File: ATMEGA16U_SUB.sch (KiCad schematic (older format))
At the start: 14 parts, among them J2 ICSP1, U5 ATmega16U2-MU, Y1 16MHz

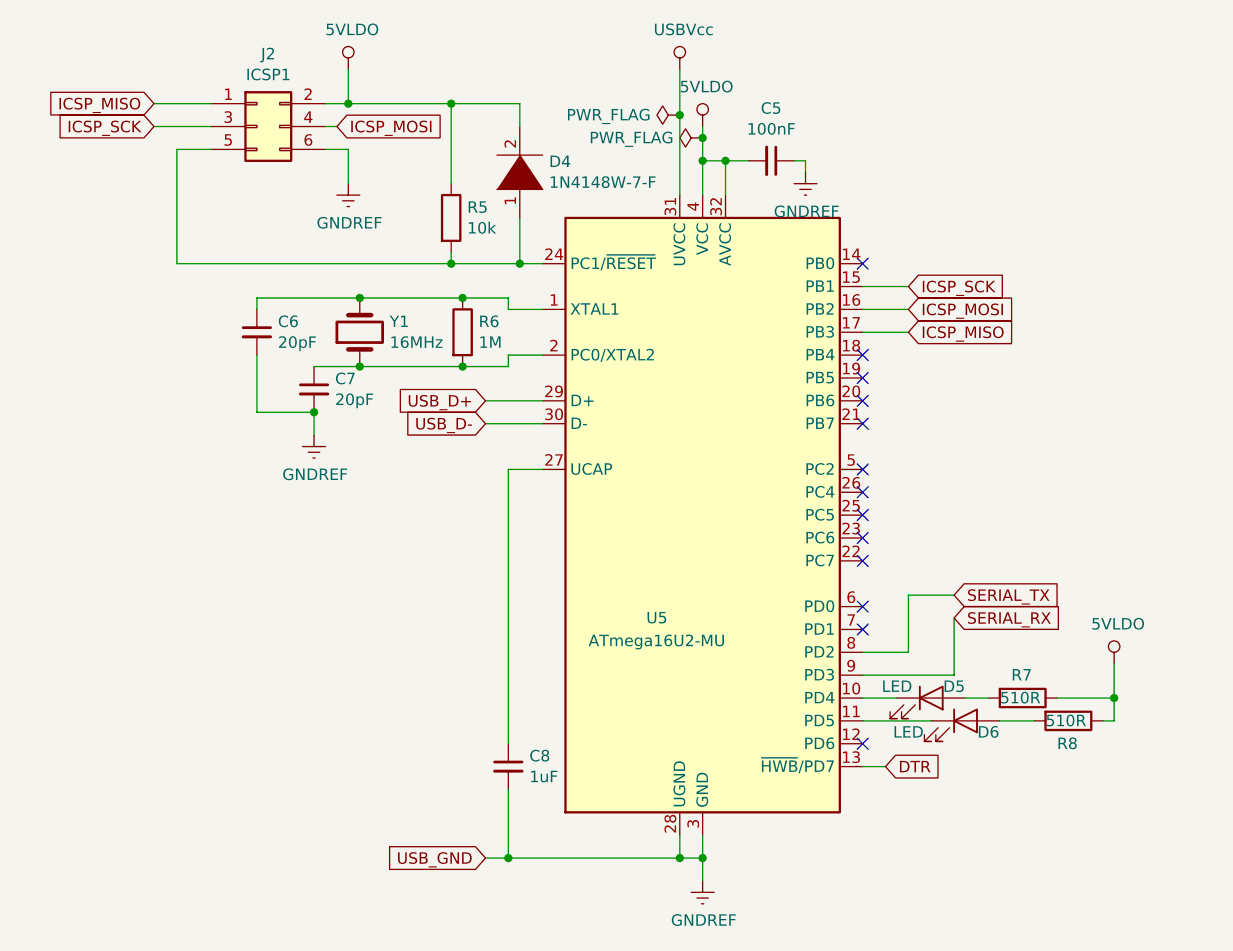
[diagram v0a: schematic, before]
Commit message: Set component footprints, added datasheets, fixed the last DRC error and a couple component values
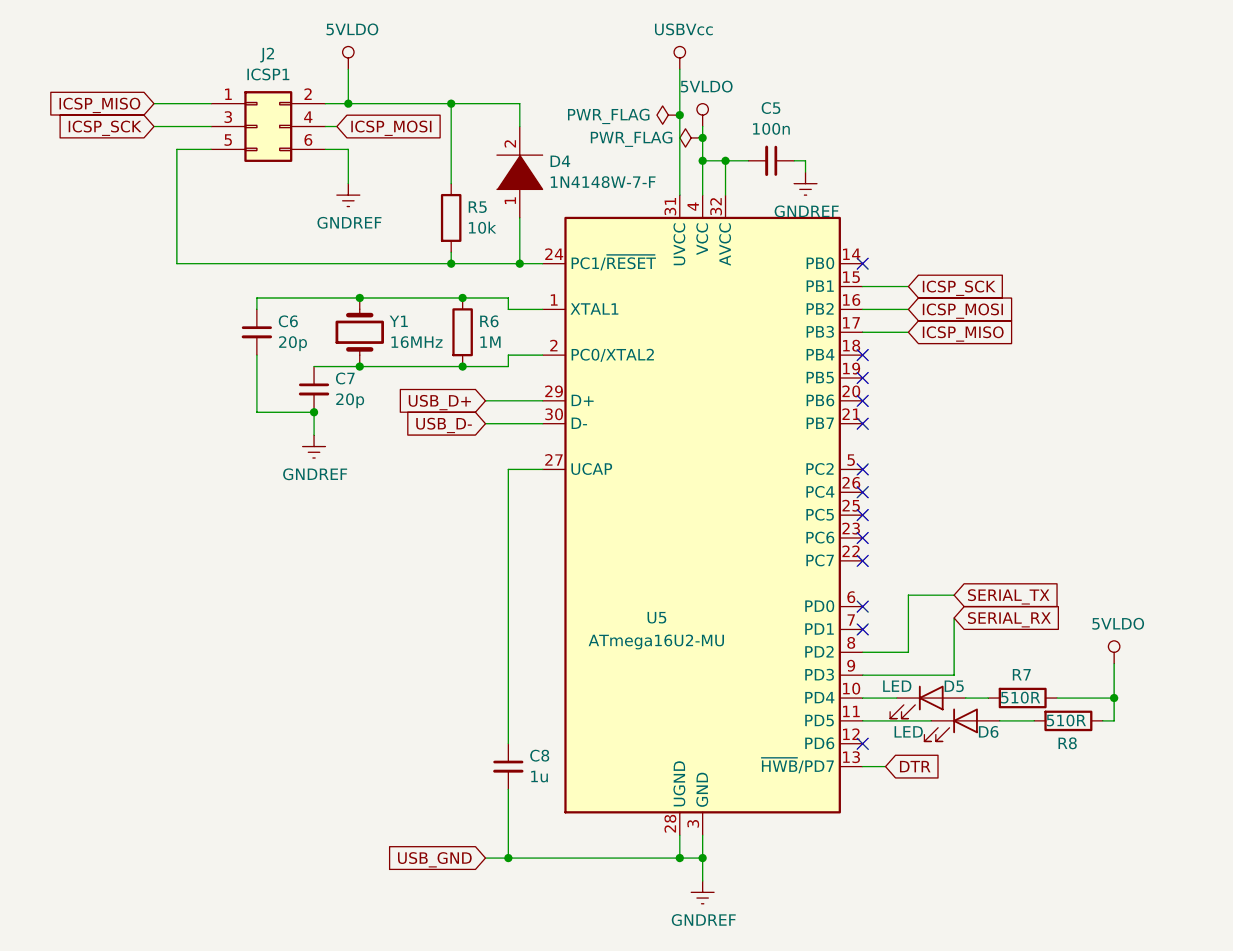
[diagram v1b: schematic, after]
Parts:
- C5: value 100nF -> 100n; footprint (none) -> Capacitor_SMD:C_0603_1608Metric
- C6, C7: value 20pF -> 20p; footprint (none) -> Capacitor_SMD:C_0603_1608Metric
- C8: value 1uF -> 1u; footprint (none) -> Capacitor_SMD:C_0603_1608Metric
- D4: footprint (none) -> Diode_SMD:D_SOD-123
- D5, D6: footprint (none) -> Diode_SMD:D_0603_1608Metric
- J2: footprint (none) -> Connector_PinHeader_2.54mm:PinHeader_2x03_P2.54mm_Vertical
- R5, R6, R7, R8: footprint (none) -> Resistor_SMD:R_0603_1608Metric
- Y1: footprint (none) -> Crystal:Crystal_SMD_SeikoEpson_MA505-2Pin_12.7x5.1mm
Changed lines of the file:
@@
 F 1 "ATmega16U2-MU" H 5550 3350 50  0000 C CNN
 F 2 "Package_DFN_QFN:QFN-32-1EP_5x5mm_P0.5mm_EP3.1x3.1mm" H 5750 3900 50  0001 C CIN
-F 3 "http://ww1.microchip.com/downloads/en/DeviceDoc/doc7799.pdf" H 5750 3900 50  0001 C CNN
+F 3 "http://www.farnell.com/datasheets/1731388.pdf" H 5750 3900 50  0001 C CNN
 	1    5750 3900
 	1    0    0    -1
@@
 F 0 "J2" H 3850 2517 50  0000 C CNN
 F 1 "ICSP1" H 3850 2426 50  0000 C CNN
-F 2 "" H 3800 2200 50  0001 C CNN
+F 2 "Connector_PinHeader_2.54mm:PinHeader_2x03_P2.54mm_Vertical" H 3800 2200 50  0001 C CNN
 F 3 "~" H 3800 2200 50  0001 C CNN
 	1    3800 2200
@@
 F 0 "R5" H 4720 2646 50  0000 L CNN
 F 1 "10k" H 4720 2555 50  0000 L CNN
-F 2 "" V 4580 2600 50  0001 C CNN
-F 3 "~" H 4650 2600 50  0001 C CNN
+F 2 "Resistor_SMD:R_0603_1608Metric" V 4580 2600 50  0001 C CNN
+F 3 "http://www.farnell.com/datasheets/2310790.pdf" H 4650 2600 50  0001 C CNN
 	1    4650 2600
 	1    0    0    -1
@@
 F 0 "D4" V 4996 2272 50  0000 R CNN
 F 1 "1N4148W-7-F" V 4905 2272 50  0000 R CNN
-F 2 "" H 4950 2400 50  0001 C CNN
-F 3 "~" H 4950 2400 50  0001 C CNN
+F 2 "Diode_SMD:D_SOD-123" H 4950 2400 50  0001 C CNN
+F 3 "http://www.farnell.com/datasheets/2238378.pdf" H 4950 2400 50  0001 C CNN
 	1    4950 2400
 	0    -1   -1   0
@@
 	5650 5300 5650 5400
 Wire Wire Line
-	5650 5400 4900 5400
-Wire Wire Line
 	5050 3700 4900 3700
 $Comp
@@
 P 4900 5000
 F 0 "C8" H 4992 5046 50  0000 L CNN
-F 1 "1uF" H 4992 4955 50  0000 L CNN
-F 2 "" H 4900 5000 50  0001 C CNN
-F 3 "~" H 4900 5000 50  0001 C CNN
+F 1 "1u" H 4992 4955 50  0000 L CNN
+F 2 "Capacitor_SMD:C_0603_1608Metric" H 4900 5000 50  0001 C CNN
+F 3 "http://www.farnell.com/datasheets/2237828.pdf" H 4900 5000 50  0001 C CNN
 	1    4900 5000
 	1    0    0    -1
@@
 P 6050 2350
 F 0 "C5" V 5821 2350 50  0000 C CNN
-F 1 "100nF" V 5912 2350 50  0000 C CNN
-F 2 "" H 6050 2350 50  0001 C CNN
-F 3 "~" H 6050 2350 50  0001 C CNN
+F 1 "100n" V 5912 2350 50  0000 C CNN
+F 2 "Capacitor_SMD:C_0603_1608Metric" H 6050 2350 50  0001 C CNN
+F 3 "http://www.farnell.com/datasheets/2739842.pdf" H 6050 2350 50  0001 C CNN
 	1    6050 2350
 	0    1    1    0
@@
 F 0 "R6" H 4770 3146 50  0000 L CNN
 F 1 "1M" H 4770 3055 50  0000 L CNN
-F 2 "" V 4630 3100 50  0001 C CNN
-F 3 "~" H 4700 3100 50  0001 C CNN
+F 2 "Resistor_SMD:R_0603_1608Metric" V 4630 3100 50  0001 C CNN
+F 3 "http://www.farnell.com/datasheets/2310790.pdf" H 4700 3100 50  0001 C CNN
 	1    4700 3100
 	1    0    0    -1
@@
 F 0 "Y1" V 4296 2969 50  0000 R CNN
 F 1 "16MHz" V 4205 2969 50  0000 R CNN
-F 2 "" H 4250 3100 50  0001 C CNN
-F 3 "FOXSLF/160-20e" H 4250 3100 50  0001 C CNN
+F 2 "Crystal:Crystal_SMD_SeikoEpson_MA505-2Pin_12.7x5.1mm" H 4250 3100 50  0001 C CNN
+F 3 "http://www.farnell.com/datasheets/1497895.pdf" H 4250 3100 50  0001 C CNN
 	1    4250 3100
 	0    -1   -1   0
@@
 P 4050 3350
 F 0 "C7" H 4142 3396 50  0000 L CNN
-F 1 "20pF" H 4142 3305 50  0000 L CNN
-F 2 "" H 4050 3350 50  0001 C CNN
-F 3 "~" H 4050 3350 50  0001 C CNN
+F 1 "20p" H 4142 3305 50  0000 L CNN
+F 2 "Capacitor_SMD:C_0603_1608Metric" H 4050 3350 50  0001 C CNN
+F 3 "http://www.farnell.com/datasheets/2340522.pdf" H 4050 3350 50  0001 C CNN
 	1    4050 3350
 	1    0    0    -1
@@
 P 3800 3100
 F 0 "C6" H 3892 3146 50  0000 L CNN
-F 1 "20pF" H 3892 3055 50  0000 L CNN
-F 2 "" H 3800 3100 50  0001 C CNN
-F 3 "~" H 3800 3100 50  0001 C CNN
+F 1 "20p" H 3892 3055 50  0000 L CNN
+F 2 "Capacitor_SMD:C_0603_1608Metric" H 3800 3100 50  0001 C CNN
+F 3 "http://www.farnell.com/datasheets/2340522.pdf" H 3800 3100 50  0001 C CNN
 	1    3800 3100
 	1    0    0    -1
@@
 F 0 "D5" H 6850 4750 50  0000 C CNN
 F 1 "LED" H 6600 4750 50  0000 C CNN
-F 2 "" H 6750 4700 50  0001 C CNN
-F 3 "~" H 6750 4700 50  0001 C CNN
+F 2 "Diode_SMD:D_0603_1608Metric" H 6750 4700 50  0001 C CNN
+F 3 "http://www.farnell.com/datasheets/1681524.pdf" H 6750 4700 50  0001 C CNN
 	1    6750 4700
 	1    0    0    -1
@@
 F 0 "D6" H 7000 4750 50  0000 C CNN
 F 1 "LED" H 6650 4750 50  0000 C CNN
-F 2 "" H 6900 4800 50  0001 C CNN
-F 3 "~" H 6900 4800 50  0001 C CNN
+F 2 "Diode_SMD:D_0603_1608Metric" H 6900 4800 50  0001 C CNN
+F 3 "http://www.farnell.com/datasheets/1681524.pdf" H 6900 4800 50  0001 C CNN
 	1    6900 4800
 	1    0    0    -1
@@
 F 0 "R7" V 7050 4650 50  0000 L CNN
 F 1 "510R" V 7150 4600 50  0000 L CNN
-F 2 "" V 7080 4700 50  0001 C CNN
-F 3 "~" H 7150 4700 50  0001 C CNN
+F 2 "Resistor_SMD:R_0603_1608Metric" V 7080 4700 50  0001 C CNN
+F 3 "http://www.farnell.com/datasheets/2310790.pdf" H 7150 4700 50  0001 C CNN
 	1    7150 4700
 	0    1    1    0
@@
 F 0 "R8" V 7450 4750 50  0000 L CNN
 F 1 "510R" V 7350 4700 50  0000 L CNN
-F 2 "" V 7280 4800 50  0001 C CNN
-F 3 "~" H 7350 4800 50  0001 C CNN
+F 2 "Resistor_SMD:R_0603_1608Metric" V 7280 4800 50  0001 C CNN
+F 3 "http://www.farnell.com/datasheets/2310790.pdf" H 7350 4800 50  0001 C CNN
 	1    7350 4800
 	0    1    1    0
@@
 	5750 5400 5750 5500
 $Comp
-L power:PWR_FLAG #FLG0105
+L power:PWR_FLAG #FLG05
 U 1 1 5ED9A18D
 P 5650 2150
-F 0 "#FLG0105" H 5650 2225 50  0001 C CNN
+F 0 "#FLG05" H 5650 2225 50  0001 C CNN
 F 1 "PWR_FLAG" V 5650 2277 50  0000 L CNN
 F 2 "" H 5650 2150 50  0001 C CNN
@@
 	5650 2150 5650 2500
 $Comp
-L power:PWR_FLAG #FLG0106
+L power:PWR_FLAG #FLG06
 U 1 1 5ED9A3FF
 P 5750 2250
-F 0 "#FLG0106" H 5750 2325 50  0001 C CNN
+F 0 "#FLG06" H 5750 2325 50  0001 C CNN
 F 1 "PWR_FLAG" V 5750 2377 50  0000 L CNN
 F 2 "" H 5750 2250 50  0001 C CNN
@@
 	4950 2100 4950 2200
 Connection ~ 4650 2100
+Wire Wire Line
+	4900 5400 5650 5400
 $EndSCHEMATC

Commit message: Updated the schematic, added missing footprints, started PCB design
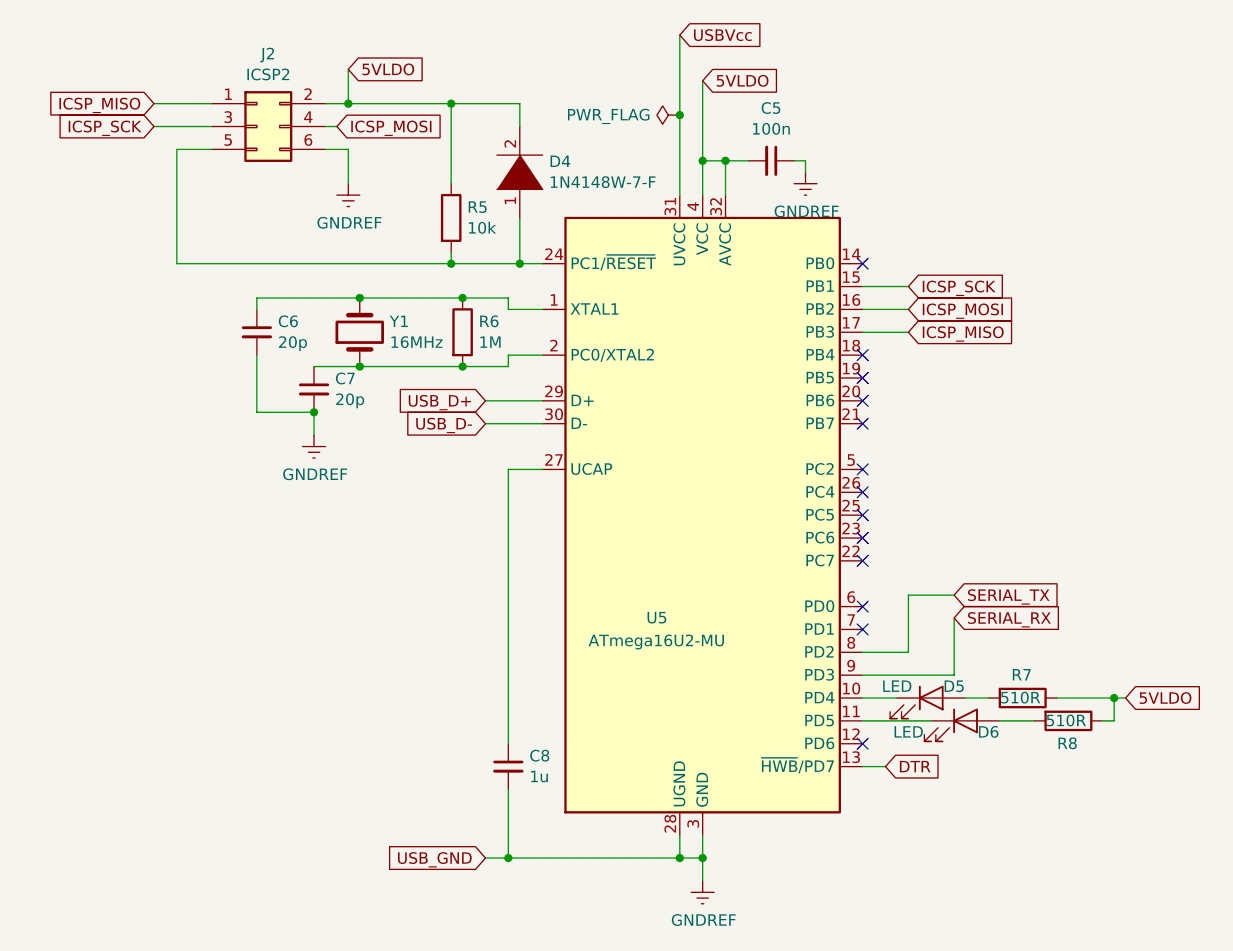
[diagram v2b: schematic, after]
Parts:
- J2: value ICSP1 -> ICSP2
- Y1: footprint Crystal:Crystal_SMD_SeikoEpson_MA505-2Pin_12.7x5.1mm -> footprints:HC-49S
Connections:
- net 5VLDO: now reaches R7.1, R8.1
- net 5VLDO: now also C5.2, D4.2 (A), J2.2 (Pin_2), R5.1, U5.32 (AVCC), U5.4 (VCC)
- net USBVcc: now reaches U5.31 (UVCC)
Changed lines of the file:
@@
 Wire Wire Line
 	5850 2350 5750 2350
-$Comp
-L power_symbols:5VLDO #PWR018
-U 1 1 5EC8208E
-P 5750 2200
-F 0 "#PWR018" H 5750 2050 50  0001 C CNN
-F 1 "5VLDO" H 5767 2373 50  0000 C CNN
-F 2 "" H 5750 2200 50  0001 C CNN
-F 3 "" H 5750 2200 50  0001 C CNN
-	1    5750 2200
-	1    0    0    -1
-$EndComp
-Wire Wire Line
-	5750 2200 5750 2250
 Connection ~ 5750 2350
-$Comp
-L power_symbols:5VLDO #PWR016
-U 1 1 5EC825EF
-P 4200 1950
-F 0 "#PWR016" H 4200 1800 50  0001 C CNN
-F 1 "5VLDO" H 4217 2123 50  0000 C CNN
-F 2 "" H 4200 1950 50  0001 C CNN
-F 3 "" H 4200 1950 50  0001 C CNN
-	1    4200 1950
-	1    0    0    -1
-$EndComp
 $Comp
 L Connector_Generic:Conn_02x03_Odd_Even J2
@@
 P 3800 2200
 F 0 "J2" H 3850 2517 50  0000 C CNN
-F 1 "ICSP1" H 3850 2426 50  0000 C CNN
+F 1 "ICSP2" H 3850 2426 50  0000 C CNN
 F 2 "Connector_PinHeader_2.54mm:PinHeader_2x03_P2.54mm_Vertical" H 3800 2200 50  0001 C CNN
 F 3 "~" H 3800 2200 50  0001 C CNN
@@
 Wire Wire Line
 	4950 2800 5050 2800
-$Comp
-L power_symbols:USBVcc #PWR017
-U 1 1 5EC8A901
-P 5650 1950
-F 0 "#PWR017" H 5650 1800 50  0001 C CNN
-F 1 "USBVcc" H 5667 2123 50  0000 C CNN
-F 2 "" H 5650 1950 50  0001 C CNN
-F 3 "" H 5650 1950 50  0001 C CNN
-	1    5650 1950
-	1    0    0    -1
-$EndComp
-Wire Wire Line
-	5650 1950 5650 2150
 Text GLabel 4800 3400 0    50   Input ~ 0
 USB_D+
@@
 F 0 "Y1" V 4296 2969 50  0000 R CNN
 F 1 "16MHz" V 4205 2969 50  0000 R CNN
-F 2 "Crystal:Crystal_SMD_SeikoEpson_MA505-2Pin_12.7x5.1mm" H 4250 3100 50  0001 C CNN
+F 2 "footprints:HC-49S" H 4250 3100 50  0001 C CNN
 F 3 "http://www.farnell.com/datasheets/1497895.pdf" H 4250 3100 50  0001 C CNN
 	1    4250 3100
@@
 Wire Wire Line
 	7000 4700 6900 4700
-$Comp
-L power_symbols:5VLDO #PWR022
-U 1 1 5EBFF36E
-P 7550 4550
-F 0 "#PWR022" H 7550 4400 50  0001 C CNN
-F 1 "5VLDO" H 7567 4723 50  0000 C CNN
-F 2 "" H 7550 4550 50  0001 C CNN
-F 3 "" H 7550 4550 50  0001 C CNN
-	1    7550 4550
-	1    0    0    -1
-$EndComp
-Wire Wire Line
-	7550 4550 7550 4700
 Wire Wire Line
 	7550 4700 7300 4700
@@
 Wire Wire Line
 	7550 4800 7550 4700
-Connection ~ 7550 4700
 Wire Wire Line
 	6450 5000 6550 5000
@@
 Wire Wire Line
 	5650 2150 5650 2500
-$Comp
-L power:PWR_FLAG #FLG06
-U 1 1 5ED9A3FF
-P 5750 2250
-F 0 "#FLG06" H 5750 2325 50  0001 C CNN
-F 1 "PWR_FLAG" V 5750 2377 50  0000 L CNN
-F 2 "" H 5750 2250 50  0001 C CNN
-F 3 "~" H 5750 2250 50  0001 C CNN
-	1    5750 2250
-	0    -1   -1   0
-$EndComp
-Connection ~ 5750 2250
-Wire Wire Line
-	5750 2250 5750 2350
 Wire Wire Line
 	4650 2100 4650 2450
@@
 Wire Wire Line
 	4900 5400 5650 5400
+Text GLabel 4200 1950 2    50   Input ~ 0
+5VLDO
+Text GLabel 5750 2000 2    50   Input ~ 0
+5VLDO
+Text GLabel 5650 1800 2    50   Input ~ 0
+USBVcc
+Wire Wire Line
+	5650 1800 5650 2150
+Text GLabel 7600 4700 2    50   Input ~ 0
+5VLDO
+Wire Wire Line
+	7550 4700 7600 4700
+Connection ~ 7550 4700
+Wire Wire Line
+	5750 2000 5750 2350
 $EndSCHEMATC
